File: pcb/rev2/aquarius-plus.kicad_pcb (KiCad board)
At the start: 2 copper layers, 167 x 115 mm, 170 parts, among them J1 Power in, J10 FPGA spare, J11 Hand controller 2, J12 Hand controller 1, J13 ESP32 spare, J2 ESP USB Host, J3 Audio out, J4 VGA, J5 Cassette out, J6 Cassette in, J7 Expansion port, J8 Printer, J9 TF-03A, Q1 BC847C, Q2 BC847C, Q3 2N7002, SW1 SW_DPDT_x2, U1 SN74AHCT1G125DBVR, U10 ESP32-S3-WROOM-1-N4R2, U11 LDL1117S33R, U12 SN74CB3T3245PWR, U13 IS61C5128AS-25QLI, U2 SN74AHCT1G125DBVR, U3 LD1117S12, U4 SN74CB3T3245PWR, U5 MAX3221ECPWR, U6 XC6SLX9-2TQG144C, U7 Z84C0010AEG, U8 SN74CB3T3245PWR, U9 SN74CB3T3245PWR, X1 SX3M14.31818M20F30TNN

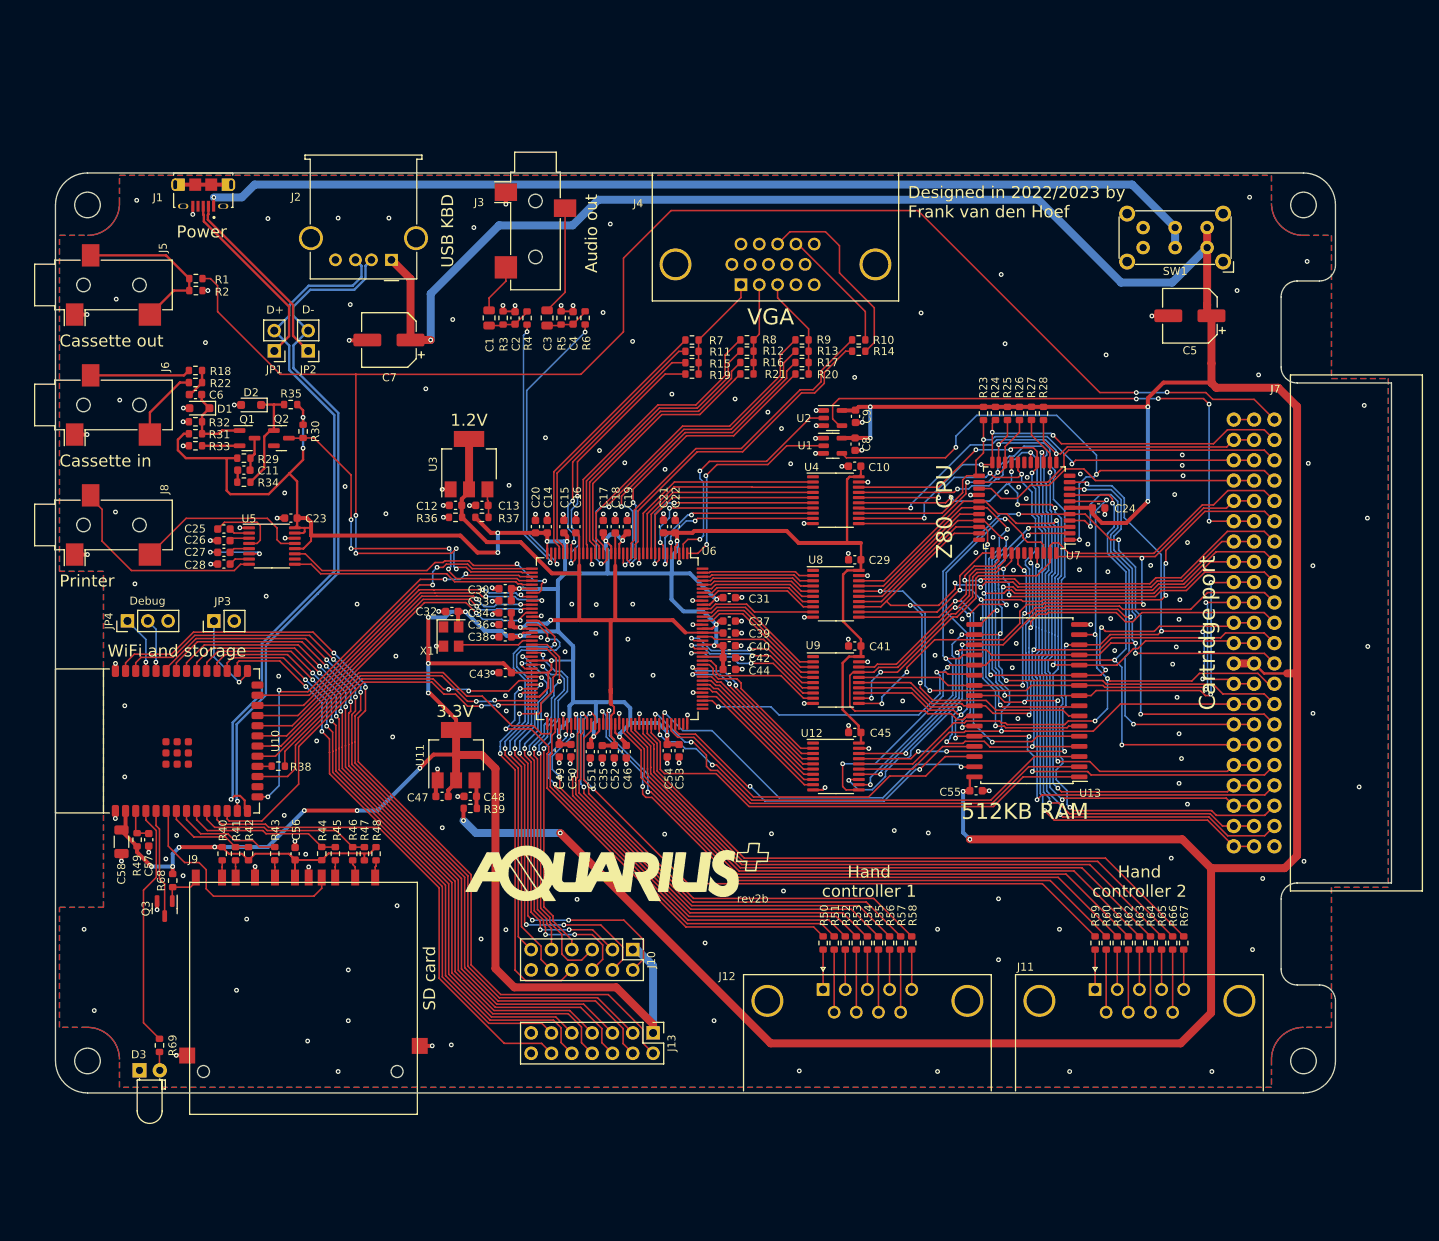
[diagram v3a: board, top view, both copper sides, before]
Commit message: rev2 PCB Labels / remove rev2b
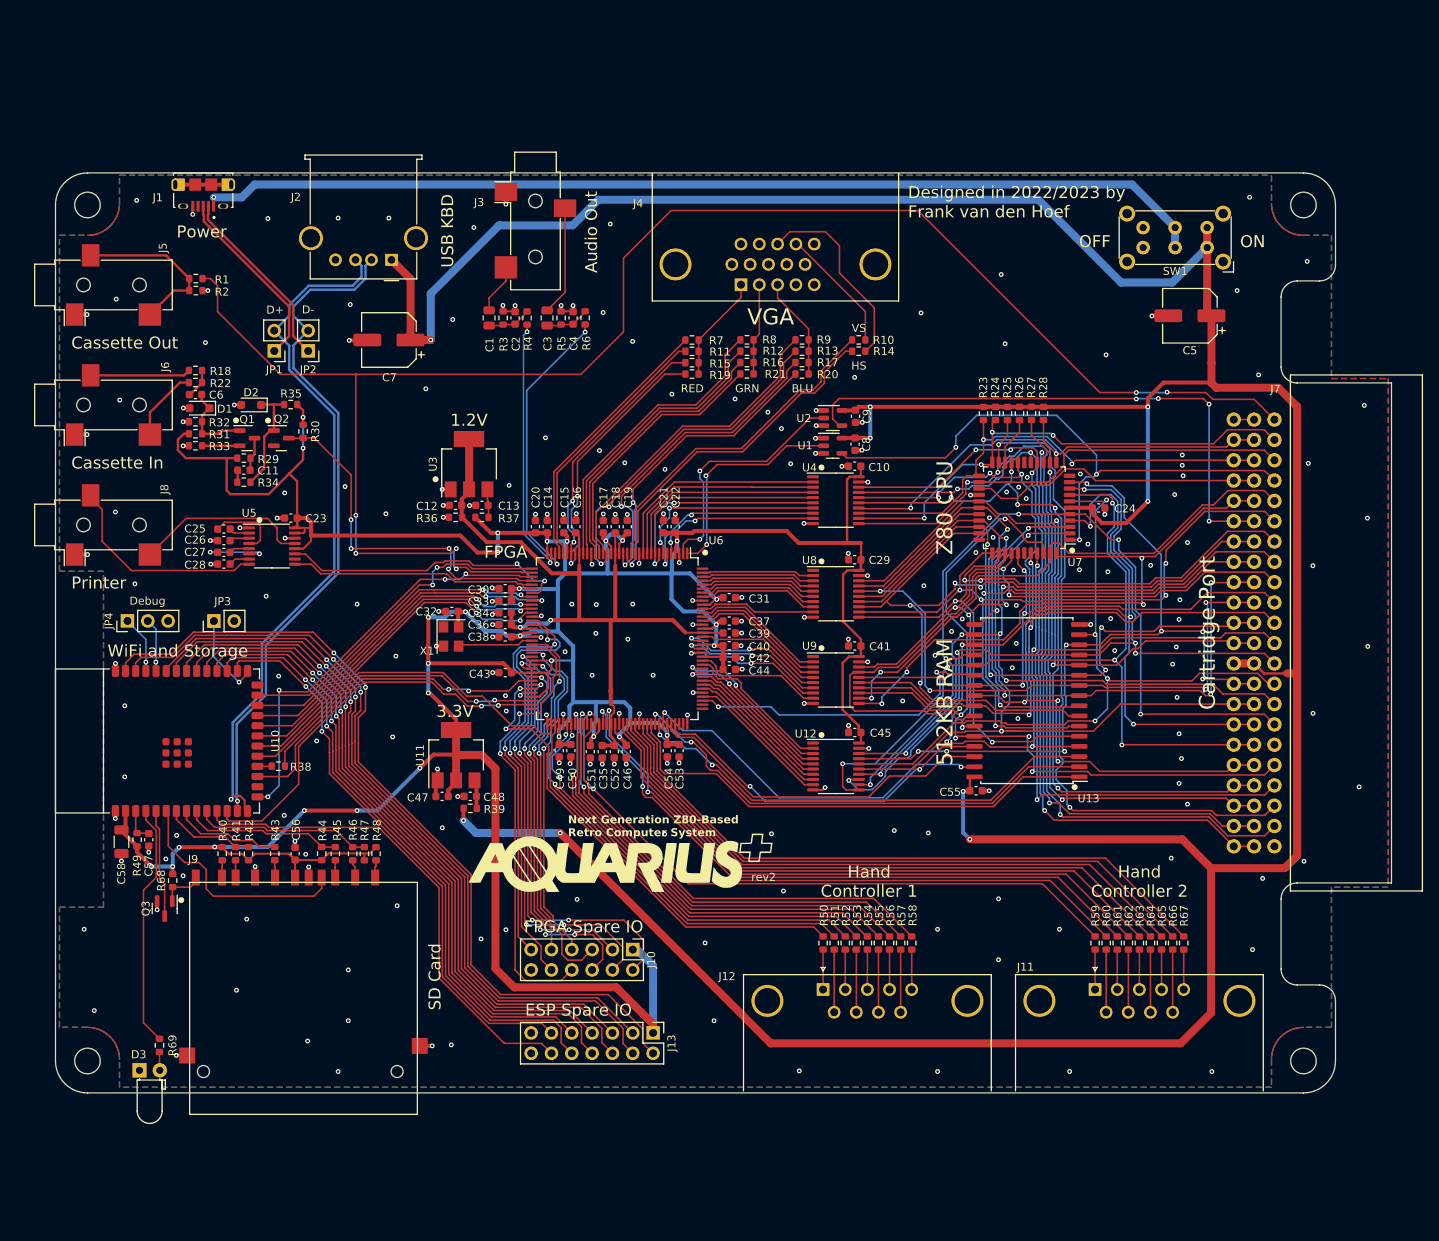
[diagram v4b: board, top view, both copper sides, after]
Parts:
- J3: value Audio out -> Audio Out
- J5: value Cassette out -> Cassette Out
- J6: value Cassette in -> Cassette In
- moved #G1 1.22 mm to (135.6, 121.2)
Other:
- board text added: "Audio Out"
- board text added: "BLU"
- board text added: "Cartridge Port"
- board text added: "Cassette In"
- board text added: "Cassette Out"
- board text added: "ESP Spare IO"
- board text added: "FPGA"
- board text added: "FPGA Spare IO"
- board text added: "GRN"
- board text added: "HS"
- board text added: "Hand Controller 1"
- board text added: "Hand Controller 2"
- board text added: "Next Generation Z80-Based Retro Computer System"
- board text added: "OFF"
- board text added: "ON"
- board text added: "RED"
- board text added: "SD Card"
- board text added: "VS"
- board text added: "WiFi and Storage"
- board text added: "rev2"
- board text removed: "Audio out"
- board text removed: "Cartridge port"
- board text removed: "Cassette in"
- board text removed: "Cassette out"
- board text removed: "Hand controller 1"
- board text removed: "Hand controller 2"
- board text removed: "SD card"
- board text removed: "WiFi and storage"
- board text removed: "rev2b"
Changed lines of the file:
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@@
     (property "ki_keywords" "serial UART RS232")
     (attr smd)
-    (fp_text reference "U5" (at -2.880304 -3.428997) (layer "F.SilkS")
+    (fp_text reference "U5" (at -2.845491 -4.124246) (layer "F.SilkS")
         (effects (font (size 1 1) (thickness 0.15)))
     )
@@
     (property "ki_keywords" "SRAM MEMORY")
     (attr smd)
-    (fp_text reference "U13" (at -7.90898 -11.547977 180) (layer "F.SilkS")
+    (fp_text reference "U13" (at -7.711158 -12.231139 180) (layer "F.SilkS")
         (effects (font (size 1 1) (thickness 0.15)))
     )
@@
   )
   (footprint "aquarius-plus:aqplus_logo" locked (layer "F.Cu")
-    (at 135.181646 122.373963)
+    (at 135.599907 121.22734)
     (attr board_only exclude_from_pos_files exclude_from_bom)
     (fp_text reference "#G1" (at 0 -4) (layer "F.SilkS") hide
@@
     (property "Sheetname" "")
     (attr smd)
-    (fp_text reference "U6" (at -10.943419 -11.480905) (layer "F.SilkS")
+    (fp_text reference "U6" (at -12.270111 -12.347986) (layer "F.SilkS")
         (effects (font (size 1 1) (thickness 0.15)))
     )
@@
         (effects (font (size 1 1) (thickness 0.15)))
     )
-    (fp_text value "Cassette in" (at 0 10.35 90) (layer "F.Fab")
+    (fp_text value "Cassette In" (at 0 10.35 90) (layer "F.Fab")
         (effects (font (size 1 1) (thickness 0.15)))
     )
@@
     (property "ki_keywords" "Z80")
     (attr smd)
-    (fp_text reference "U7" (at -6.132075 -5.978522 180) (layer "F.SilkS")
+    (fp_text reference "U7" (at -6.330859 -6.829909 180) (layer "F.SilkS")
         (effects (font (size 1 1) (thickness 0.15)))
     )
@@
     (property "Sheetname" "")
     (attr smd)
-    (fp_text reference "U4" (at -3.030303 -4.134344) (layer "F.SilkS")
+    (fp_text reference "U4" (at -3.296876 -4.06905) (layer "F.SilkS")
         (effects (font (size 1 1) (thickness 0.15)))
     )
@@
     (property "Sheetname" "")
     (attr smd)
-    (fp_text reference "U9" (at -2.85769 -4.314247) (layer "F.SilkS")
+    (fp_text reference "U9" (at -3.310276 -4.248953) (layer "F.SilkS")
         (effects (font (size 1 1) (thickness 0.15)))
     )
@@
     (property "Sheetname" "")
     (attr smd)
-    (fp_text reference "U8" (at -2.532069 -4.239011) (layer "F.SilkS")
+    (fp_text reference "U8" (at -3.310276 -4.173717) (layer "F.SilkS")
         (effects (font (size 1 1) (thickness 0.15)))
     )
@@
     (property "Sheetname" "")
     (attr smd)
-    (fp_text reference "U12" (at -3.031335 -4.152751) (layer "F.SilkS")
+    (fp_text reference "U12" (at -3.786467 -4.087457) (layer "F.SilkS")
         (effects (font (size 1 1) (thickness 0.15)))
     )
@@
         (effects (font (size 1 1) (thickness 0.15)))
     )
-    (fp_text value "Audio out" (at 0 10.35) (layer "F.Fab")
+    (fp_text value "Audio Out" (at 0 10.35) (layer "F.Fab")
         (effects (font (size 1 1) (thickness 0.15)))
     )
@@
         (effects (font (size 1 1) (thickness 0.15)))
     )
-    (fp_text value "Cassette out" (at 0 10.35 90) (layer "F.Fab")
+    (fp_text value "Cassette Out" (at 0 10.35 90) (layer "F.Fab")
         (effects (font (size 1 1) (thickness 0.15)))
     )
@@
     )
   )
+  (gr_circle (center 87.562938 65.930888) (end 87.862938 65.930888)
+    (stroke (width 0.15) (type solid)) (fill solid) (layer "F.SilkS"))
+  (gr_circle (center 80.718128 125.890806) (end 81.018128 125.890806)
+    (stroke (width 0.15) (type solid)) (fill solid) (layer "F.SilkS"))
+  (gr_circle (center 90.498608 78.380775) (end 90.798608 78.380775)
+    (stroke (width 0.15) (type solid)) (fill solid) (layer "F.SilkS"))
+  (gr_circle (center 192.395702 111.77155) (end 192.695702 111.77155)
+    (stroke (width 0.15) (type solid)) (fill solid) (layer "F.SilkS"))
+  (gr_circle (center 112.51359 73.282783) (end 112.81359 73.282783)
+    (stroke (width 0.15) (type solid)) (fill solid) (layer "F.SilkS"))
+  (gr_circle (center 160.750048 83.550539) (end 161.050048 83.550539)
+    (stroke (width 0.15) (type solid)) (fill solid) (layer "F.SilkS"))
+  (gr_circle (center 192.084089 82.185583) (end 192.384089 82.185583)
+    (stroke (width 0.15) (type solid)) (fill solid) (layer "F.SilkS"))
+  (gr_circle (center 146.204452 82.448383) (end 146.504452 82.448383)
+    (stroke (width 0.15) (type solid)) (fill solid) (layer "F.SilkS"))
+  (gr_circle (center 160.750048 105.247532) (end 161.050048 105.247532)
+    (stroke (width 0.15) (type solid)) (fill solid) (layer "F.SilkS"))
+  (gr_circle (center 160.750048 71.813511) (end 161.050048 71.813511)
+    (stroke (width 0.15) (type solid)) (fill solid) (layer "F.SilkS"))
+  (gr_circle (center 160.750048 94.392676) (end 161.050048 94.392676)
+    (stroke (width 0.15) (type solid)) (fill solid) (layer "F.SilkS"))
+  (gr_circle (center 91.565353 65.944456) (end 91.865353 65.944456)
+    (stroke (width 0.15) (type solid)) (fill solid) (layer "F.SilkS"))
   (gr_line (start 227.5 39) (end 227.5 146)
     (stroke (width 0.15) (type solid)) (layer "Dwgs.User"))
@@
   (gr_line (start 223 48.5) (end 220.2 48.5)
     (stroke (width 0.1) (type solid)) (layer "Edge.Cuts"))
-  (gr_text "Hand\ncontroller 1" (at 166.706608 123.574589) (layer "F.SilkS")
+  (gr_text "Hand\nController 1" (at 166.706608 123.574589) (layer "F.SilkS")
     (effects (font (size 1.5 1.5) (thickness 0.3)))
   )
+  (gr_text "VS" (at 165.427459 54.40568) (layer "F.SilkS")
+    (effects (font (size 1 1) (thickness 0.15)))
+  )
+  (gr_text "RED" (at 144.59603 61.948934) (layer "F.SilkS")
+    (effects (font (size 1 1) (thickness 0.15)))
+  )
   (gr_text "Designed in 2022/2023 by\nFrank van den Hoef" (at 171.55 38.65) (layer "F.SilkS")
     (effects (font (size 1.5 1.5) (thickness 0.3)) (justify left))
   )
-  (gr_text "Z80 CPU" (at 176.1475 77.318099 90) (layer "F.SilkS")
+  (gr_text "Z80 CPU" (at 176.180877 76.842951 90) (layer "F.SilkS")
     (effects (font (size 2 2) (thickness 0.3)))
   )
-  (gr_text "Cassette out" (at 65.5 56) (layer "F.SilkS")
+  (gr_text "Cassette Out" (at 66.970031 56.249555) (layer "F.SilkS")
     (effects (font (size 1.5 1.5) (thickness 0.3)) (justify left))
   )
-  (gr_text "SD card" (at 111.76 139.7 90) (layer "F.SilkS")
+  (gr_text "SD Card" (at 112.434987 139.671126 90) (layer "F.SilkS")
     (effects (font (size 1.5 1.5) (thickness 0.3)) (justify left))
   )
@@
     (effects (font (size 1 1) (thickness 0.15)))
   )
-  (gr_text "Hand\ncontroller 2" (at 200.499878 123.574589) (layer "F.SilkS")
+  (gr_text "FPGA Spare IO" (at 131.021301 129.228383) (layer "F.SilkS")
+    (effects (font (size 1.5 1.5) (thickness 0.3)))
+  )
+  (gr_text "Hand\nController 2" (at 200.499878 123.574589) (layer "F.SilkS")
     (effects (font (size 1.5 1.5) (thickness 0.3)))
   )
-  (gr_text "WiFi and storage" (at 71.5 94.75) (layer "F.SilkS")
+  (gr_text "WiFi and Storage" (at 71.5 94.75) (layer "F.SilkS")
     (effects (font (size 1.5 1.5) (thickness 0.3)) (justify left))
   )
-  (gr_text "Cassette in" (at 65.5 71) (layer "F.SilkS")
+  (gr_text "ON" (at 214.652084 43.58135) (layer "F.SilkS")
+    (effects (font (size 1.5 1.5) (thickness 0.3)))
+  )
+  (gr_text "Cassette In" (at 66.970031 71.249555) (layer "F.SilkS")
     (effects (font (size 1.5 1.5) (thickness 0.3)) (justify left))
   )
@@
     (effects (font (size 1.5 1.5) (thickness 0.3)))
   )
-  (gr_text "Audio out" (at 132 47.5 90) (layer "F.SilkS")
+  (gr_text "Audio Out" (at 132 47.5 90) (layer "F.SilkS")
     (effects (font (size 1.5 1.5) (thickness 0.3)) (justify left))
   )
-  (gr_text "Cartridge port" (at 209 92.5 90) (layer "F.SilkS")
+  (gr_text "HS" (at 165.427459 59.113606) (layer "F.SilkS")
+    (effects (font (size 1 1) (thickness 0.15)))
+  )
+  (gr_text "FPGA" (at 121.294148 82.401391) (layer "F.SilkS")
+    (effects (font (size 1.5 1.5) (thickness 0.3)))
+  )
+  (gr_text "GRN" (at 151.475818 61.948934) (layer "F.SilkS")
+    (effects (font (size 1 1) (thickness 0.15)))
+  )
+  (gr_text "Cartridge Port" (at 209 92.5 90) (layer "F.SilkS")
     (effects (font (size 2 2) (thickness 0.3)))
   )
@@
     (effects (font (size 1 1) (thickness 0.125)) (justify left))
   )
-  (gr_text "rev2b" (at 152.154192 125.73) (layer "F.SilkS")
+  (gr_text "BLU" (at 158.376593 61.948934) (layer "F.SilkS")
+    (effects (font (size 1 1) (thickness 0.15)))
+  )
+  (gr_text "OFF" (at 194.916444 43.58135) (layer "F.SilkS")
+    (effects (font (size 1.5 1.5) (thickness 0.3)))
+  )
+  (gr_text "rev2" (at 153.510929 123.027791) (layer "F.SilkS")
     (effects (font (size 1 1) (thickness 0.15)))
   )
-  (gr_text "512KB RAM" (at 186.178943 114.815141) (layer "F.SilkS")
+  (gr_text "512KB RAM" (at 176.180877 101.149994 90) (layer "F.SilkS")
     (effects (font (size 2 2) (thickness 0.3)))
   )
@@
     (effects (font (size 1.5 1.5) (thickness 0.3)) (justify left))
   )
-  (gr_text "Printer" (at 65.5 86) (layer "F.SilkS")
+  (gr_text "ESP Spare IO" (at 130.378444 139.645687) (layer "F.SilkS")
+    (effects (font (size 1.5 1.5) (thickness 0.3)))
+  )
+  (gr_text "Next Generation Z80-Based\nRetro Computer System" (at 129.058882 116.640038) (layer "F.SilkS")
+    (effects (font (size 1 1) (thickness 0.2) bold) (justify left))
+  )
+  (gr_text "Printer" (at 66.970031 86.249555) (layer "F.SilkS")
     (effects (font (size 1.5 1.5) (thickness 0.3)) (justify left))
   )
